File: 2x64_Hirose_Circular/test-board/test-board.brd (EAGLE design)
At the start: 152.4 x 165.1 mm, 55 parts

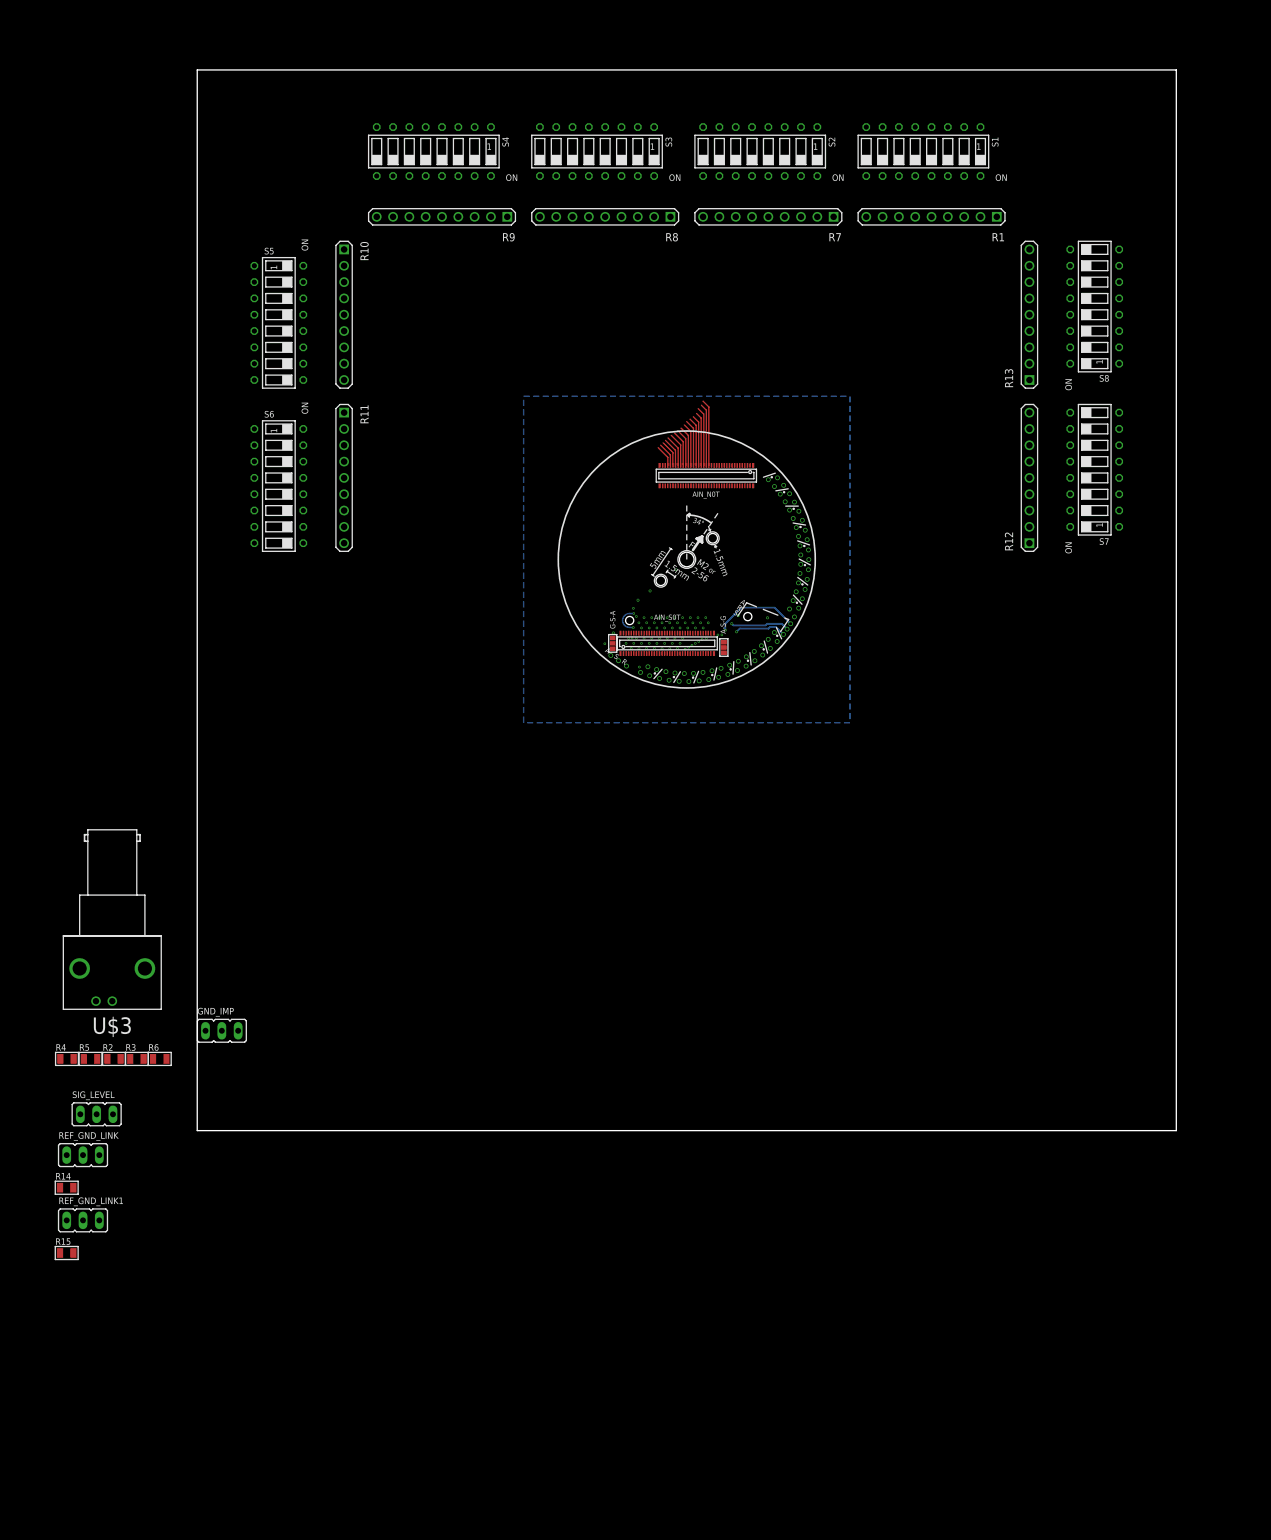
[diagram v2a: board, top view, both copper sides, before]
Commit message: Intial layout for 2x64 Hirose test board complete
- Silkscree needs work, especially for tetrode and channel labels, which
  will be very important
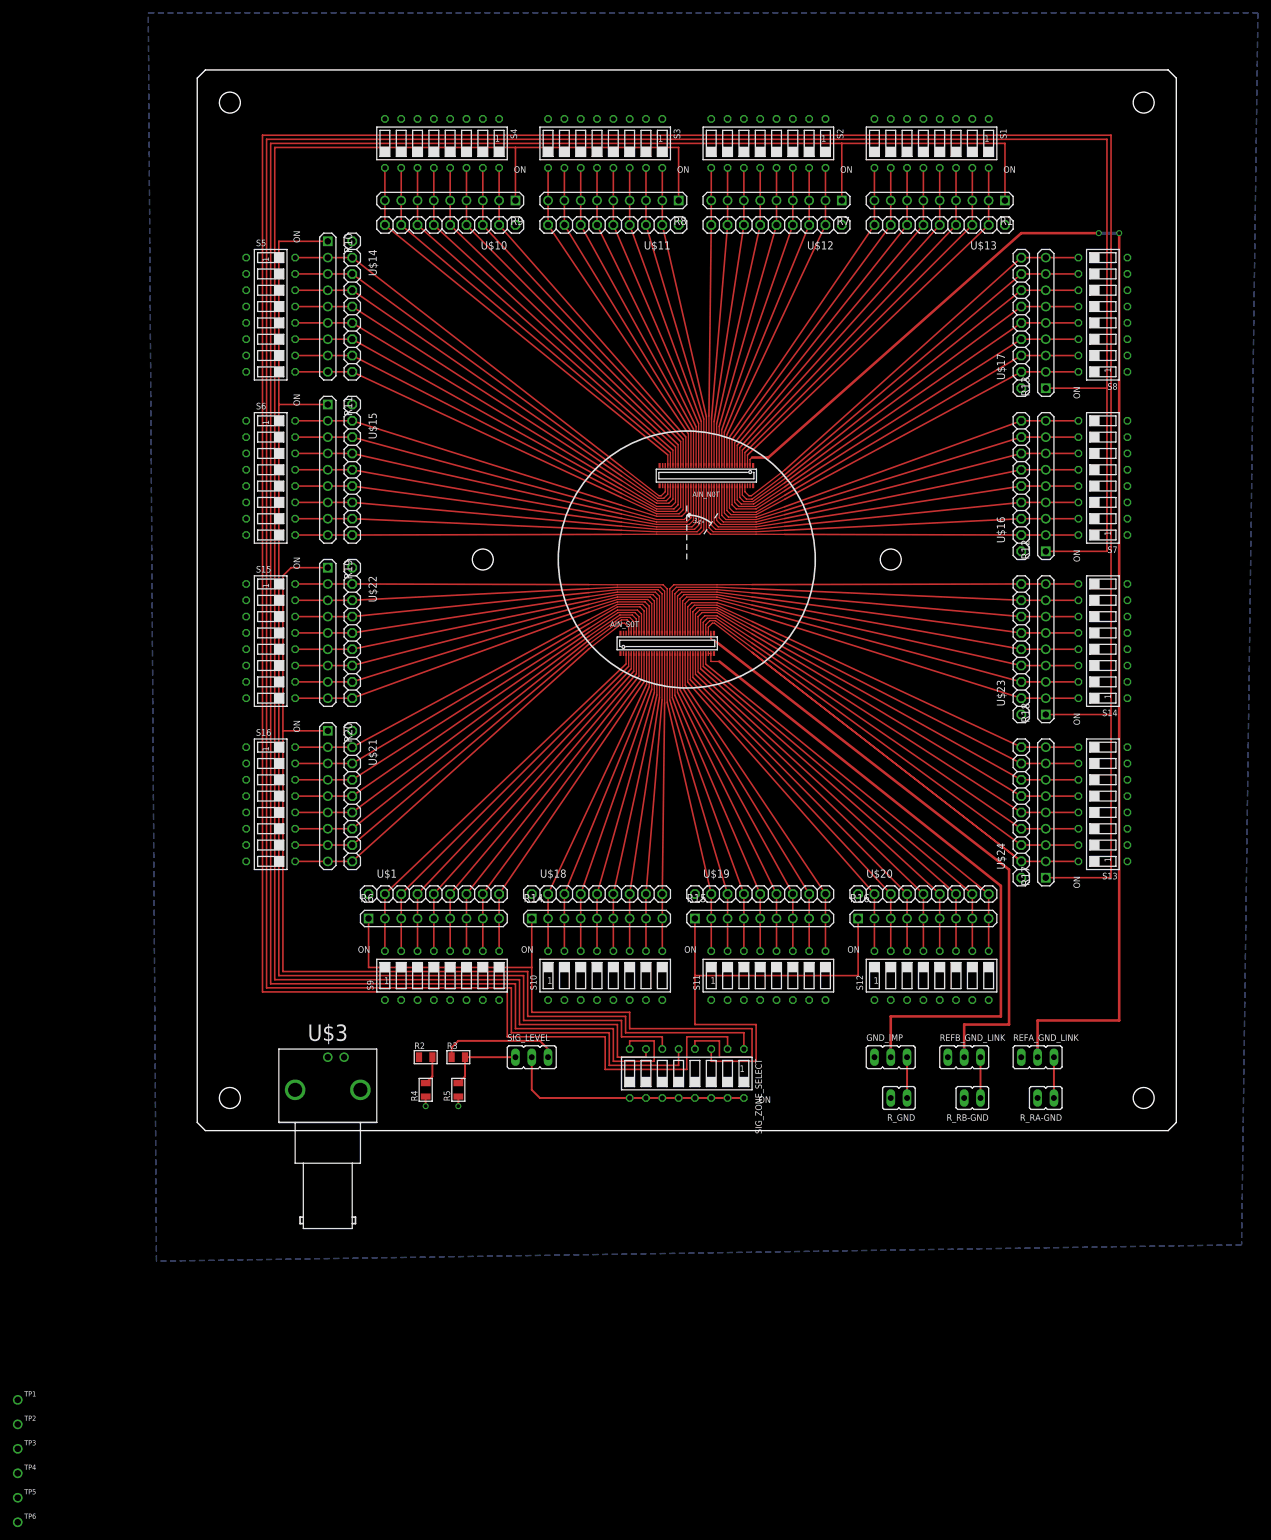
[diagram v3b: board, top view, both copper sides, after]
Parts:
- removed AGND_B0, AGND_B1, REF_B0, REF_B1, SHLD_B0, SHLD_B1: LRG_GP, jonnew:GOLDPIN_0.5ID_0.7OD
- removed REF_GND_LINK, REF_GND_LINK1: (no value), jonnew:JP3
- removed SJ_B0, SJ_B1: (no value), jonnew:SJ_2_0402
- removed TET16: 16, jonnew:TETRODE_128_0.5ID_0.7OD
- removed TET17: 17, jonnew:TETRODE_128_0.5ID_0.7OD
- removed TET18: 18, jonnew:TETRODE_128_0.5ID_0.7OD
- removed TET19: 19, jonnew:TETRODE_128_0.5ID_0.7OD
- removed TET20: 20, jonnew:TETRODE_128_0.5ID_0.7OD
- removed TET21: 21, jonnew:TETRODE_128_0.5ID_0.7OD
- removed TET22: 22, jonnew:TETRODE_128_0.5ID_0.7OD
- removed TET23: 23, jonnew:TETRODE_128_0.5ID_0.7OD
- removed TET24: 24, jonnew:TETRODE_128_0.5ID_0.7OD
- removed TET25: 25, jonnew:TETRODE_128_0.5ID_0.7OD
- removed TET26: 26, jonnew:TETRODE_128_0.5ID_0.7OD
- removed TET27: 27, jonnew:TETRODE_128_0.5ID_0.7OD
- removed TET28: 28, jonnew:TETRODE_128_0.5ID_0.7OD
- removed TET29: 29, jonnew:TETRODE_128_0.5ID_0.7OD
- removed TET30: 30, jonnew:TETRODE_128_0.5ID_0.7OD
- removed TET31: 31, jonnew:TETRODE_128_0.5ID_0.7OD
- added R16, R17, R18, R19, R20: 4609-220k, jonnew:RNX8-0.1
- added REFA_GND_LINK, REFB_GND_LINK: (no value), jonnew:JP3
- added R_GND, R_RA-GND, R_RB-GND: (no value), jonnew:JP2
- added S10, S11, S12, S13, S14, S15, S16, S9, SIG_ZONE_SELECT: (no value), jonnew:ADE008
- added TP1, TP2, TP3, TP4, TP5, TP6: (no value), jonnew:TESTPOINT
- added U$10, U$11, U$12, U$13, U$14, U$15, U$16, U$17, U$18, U$19, U$20, U$21, U$22, U$23, U$24: (no value), test-board:1X09
- AIN_S0T: device jonnew:DF40-70HEAD-EIB -> jonnew:DF40-70HEAD
- R14, R15, R6: value (none) -> 4609-220k; device jonnew:0805 -> jonnew:RNX8-0.1
- U$1: device jonnew:EIB_MOUNT_A -> test-board:1X09
- moved R15 110.8 mm to (1.27, -55.9)
- moved GND_IMP 104.2 mm to (29.2, -77.5)
- moved R14 83.6 mm to (-24.1, -55.9)
- moved U$1 70.1 mm to (-47.0, -52.1), turned to 0 degrees
- moved SIG_LEVEL 68.3 mm to (-26.7, -77.5)
- moved R5 57.5 mm to (-35.6, -82.5), turned to 90 degrees
- moved R4 56.0 mm to (-40.6, -82.5), turned to 90 degrees
- moved R3 50.0 mm to (-35.6, -77.5)
- moved R2 48.5 mm to (-40.6, -77.5)
- moved U$3 47.6 mm to (-50.8, -82.5), turned to 180 degrees
- moved R6 39.2 mm to (-49.5, -55.9)
- moved R1 2.84 mm to (49.5, 55.9)
- moved R10 2.84 mm to (-55.9, 49.5)
- moved R11 2.84 mm to (-55.9, 24.1)
- moved R12 2.84 mm to (55.9, 1.27)
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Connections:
- removed net AGND_B0: AGND_B0.P$1, AIN_S0T.69, AIN_S0T.70, SJ_B0.2
- removed net AGND_B1: AGND_B1.P$1, AIN_S0T.34, AIN_S0T.35, SJ_B1.2
- removed net N$1: R14.1, REF_GND_LINK.1
- removed net N$104: AIN_S0T.46, AIN_S0T.P46, TET26.2
- removed net N$105: AIN_S0T.47, AIN_S0T.P47, TET26.1
- removed net N$106: AIN_S0T.48, AIN_S0T.P48, TET26.0
- removed net N$107: AIN_S0T.49, AIN_S0T.P49, TET27.3
- removed net N$108: AIN_S0T.50, AIN_S0T.P50, TET27.2
- removed net N$109: AIN_S0T.51, AIN_S0T.P51, TET27.1
- removed net N$111: AIN_S0T.53, AIN_S0T.P53, TET28.3
- removed net N$112: AIN_S0T.54, AIN_S0T.P54, TET28.2
- removed net N$113: AIN_S0T.55, AIN_S0T.P55, TET28.1
- removed net N$114: AIN_S0T.56, AIN_S0T.P56, TET28.0
- removed net N$115: AIN_S0T.57, AIN_S0T.P57, TET29.3
- removed net N$116: AIN_S0T.58, AIN_S0T.P58, TET29.2
- removed net N$117: AIN_S0T.59, AIN_S0T.P59, TET29.1
- removed net N$118: AIN_S0T.60, AIN_S0T.P60, TET29.0
- removed net N$119: AIN_S0T.61, AIN_S0T.P61, TET30.3
- removed net N$120: AIN_S0T.62, AIN_S0T.P62, TET30.2
- removed net N$121: AIN_S0T.63, AIN_S0T.P63, TET30.1
- removed net N$122: AIN_S0T.64, AIN_S0T.P64, TET30.0
- removed net N$123: AIN_S0T.65, TET31.3
- removed net N$124: AIN_S0T.66, TET31.2
- removed net N$125: AIN_S0T.67, TET31.1
- removed net N$126: AIN_S0T.68, TET31.0
- removed net N$127: AIN_S0T.2, AIN_S0T.P2, TET16.3
- removed net N$128: AIN_S0T.37, AIN_S0T.P37, TET24.3
- removed net N$14: GND_IMP.1, R6.1
- removed net N$16: R4.1
- removed net N$17: R5.1
- removed net N$22: R15.1, REF_GND_LINK1.1
- removed net N$5: U$3.P$GND
- removed net N$96: AIN_S0T.38, AIN_S0T.P38, TET24.2
- removed net REF_B0: AIN_S0T.1, REF_B0.P$1
- removed net REF_B1: AIN_S0T.36, REF_B1.P$1
- new net N$130: AIN_S0T.62, R20.2, S16.15, U$21.2
- new net N$26: AIN_S0T.7, R6.6, S9.11, U$1.6
- new net N$32: AIN_S0T.9, R6.8, S9.9, U$1.8
- new net N$35: AIN_S0T.10, R14.1, S10.16, U$18.1
- new net N$41: AIN_S0T.11, R14.2, S10.15, U$18.2
- new net N$45: AIN_S0T.14, R14.5, S10.12, U$18.5
- new net N$46: AIN_S0T.15, R14.6, S10.11, U$18.6
- new net N$48: AIN_S0T.16, R14.7, S10.10, U$18.7
- new net N$49: AIN_S0T.19, R15.2, S11.15, U$19.2
- new net N$50: AIN_S0T.20, R15.3, S11.14, U$19.3
- new net N$51: AIN_S0T.21, R15.4, S11.13, U$19.4
- new net N$52: AIN_S0T.22, R15.5, S11.12, U$19.5
- new net N$53: AIN_S0T.23, R15.6, S11.11, U$19.6
- new net N$54: AIN_S0T.24, R15.7, S11.10, U$19.7
- new net N$55: AIN_S0T.25, R15.8, S11.9, U$19.8
- new net N$56: AIN_S0T.26, R16.1, S12.16, U$20.1
- new net N$58: AIN_S0T.27, R16.2, S12.15, U$20.2
- new net N$59: AIN_S0T.28, R16.3, S12.14, U$20.3
- new net N$60: AIN_S0T.29, R16.4, S12.13, U$20.4
- new net N$61: AIN_S0T.30, R16.5, S12.12, U$20.5
- new net N$62: AIN_S0T.31, R16.6, S12.11, U$20.6
- new net N$63: AIN_S0T.32, R16.7, S12.10, U$20.7
- new net N$64: AIN_S0T.33, R16.8, S12.9, U$20.8
- new net SIG_A_15-0: R12.C, R13.C, SIG_ZONE_SELECT.5
- new net SIG_A_31-16: R10.C, R11.C, SIG_ZONE_SELECT.6
- new net SIG_A_47-32: R8.C, R9.C, SIG_ZONE_SELECT.7
- new net SIG_A_63-48: R1.C, R7.C, SIG_ZONE_SELECT.8
- new net SIG_B_15-0: R19.C, R20.C, SIG_ZONE_SELECT.1
- new net SIG_B_31-16: R17.C, R18.C, SIG_ZONE_SELECT.2
- new net SIG_B_47-32: R15.C, R16.C, SIG_ZONE_SELECT.3
- new net SIG_B_63-48: R14.C, R6.C, SIG_ZONE_SELECT.4
- net GND: now also GND_IMP.1, R4.1, R5.1, REFA_GND_LINK.1, REFB_GND_LINK.1, R_GND.2, R_RA-GND.2, R_RB-GND.2, S10.1, S10.2, S10.3, S10.4, S10.5, S10.6, S10.7, S10.8, S11.1, S11.2, S11.3, S11.4, S11.5, S11.6, S11.7, S11.8, S12.1, S12.2, S12.3, S12.4, S12.5, S12.6, S12.7, S12.8, S13.1, S13.2, S13.3, S13.4, S13.5, S13.6, S13.7, S13.8, S14.1, S14.2, S14.3, S14.4, S14.5, S14.6, S14.7, S14.8, S15.1, S15.2, S15.3, S15.4, S15.5, S15.6, S15.7, S15.8, S16.1, S16.2, S16.3, S16.4, S16.5, S16.6, S16.7, S16.8, S9.1, S9.2, S9.3, S9.4, S9.5, S9.6, S9.7, S9.8, TP1.1, TP2.1, U$1.9, U$10.9, U$11.9, U$12.9, U$13.9, U$14.9, U$15.9, U$16.9, U$17.9, U$18.9, U$19.9, U$20.9, U$21.9, U$22.9, U$23.9, U$24.9, U$3.P$GND; no longer SJ_B0.1, SJ_B1.1
- net HS_GND: now also AIN_S0T.34, AIN_S0T.35; no longer AIN_N0T.34, AIN_N0T.35, AIN_N0T.69, AIN_N0T.70
- net N$10: now also U$13.2
- net N$100: now also AIN_S0T.54, R19.2, S15.15, U$22.2; no longer AIN_S0T.42, AIN_S0T.P42, TET25.2
- net N$101: now also AIN_S0T.56, R19.4, S15.13, U$22.4; no longer AIN_S0T.43, AIN_S0T.P43, TET25.1
- net N$102: now also AIN_S0T.58, R19.6, S15.11, U$22.6; no longer AIN_S0T.44, AIN_S0T.P44, TET25.0
- net N$103: now also AIN_S0T.59, R19.7, S15.10, U$22.7; no longer AIN_S0T.45, AIN_S0T.P45, TET26.3
- net N$11: now also U$12.3
- net N$110: now also AIN_S0T.13, R14.4, S10.13, U$18.4; no longer AIN_S0T.52, AIN_S0T.P52, TET27.0
- net N$12: now also U$13.3
- net N$13: now also U$12.1
- net N$15: now also REFA_GND_LINK.3, R_RA-GND.1; no longer GND_IMP.3, R6.2
- net N$18: now also U$13.6
- net N$19: now also U$13.7
- net N$2: now also GND_IMP.3, R_GND.1; no longer R14.2, REF_GND_LINK.3
- net N$20: now also U$13.5
- net N$206: now also U$10.1
- net N$207: now also U$11.8
- net N$21: now also U$13.1
- net N$210: now also U$11.5
- net N$212: now also U$11.3
- net N$214: now also U$11.1
- net N$216: now also U$12.7
- net N$219: now also U$12.4
- net N$221: now also U$12.2
- net N$23: now also U$10.2
- net N$230: now also U$13.4
- net N$231: now also U$14.2
- net N$233: now also U$14.4
- net N$235: now also U$14.6
- net N$237: now also U$14.8
- net N$238: now also U$15.1
- net N$239: now also U$15.2
- net N$24: now also U$10.4
- net N$241: now also U$15.4
- net N$242: now also U$15.5
- net N$243: now also U$15.6
- net N$245: now also U$15.7
- net N$247: now also U$16.2
- net N$248: now also U$16.3
- net N$249: now also U$16.4
- net N$25: now also U$14.7
- net N$250: now also U$16.5
- net N$251: now also U$16.6
- net N$252: now also U$16.7
- net N$253: now also U$16.8
- net N$254: now also U$17.1
- net N$255: now also U$17.2
- net N$256: now also U$17.3
- net N$257: now also U$17.4
- net N$258: now also U$17.5
- net N$259: now also U$17.6
- net N$260: now also U$17.7
- net N$261: now also U$17.8
- net N$27: now also U$10.7
- net N$28: now also REFB_GND_LINK.3, R_RB-GND.1; no longer R15.2, REF_GND_LINK1.3
- net N$29: now also U$10.5
- net N$3: now also AIN_S0T.3, R6.2, S9.15, U$1.2; no longer SHLD_B0.P$1, SJ_B0.COM
- net N$30: now also U$14.5
- net N$31: now also U$10.3
- net N$33: now also U$14.3
- net N$34: now also U$10.6
- net N$36: now also U$10.8
- net N$37: now also U$14.1
- net N$38: now also U$11.2
- net N$39: now also U$15.8
- net N$4: now also AIN_S0T.5, R6.4, S9.13, U$1.4; no longer SHLD_B1.P$1, SJ_B1.COM
- net N$40: now also U$11.4
- net N$42: now also U$11.6
- net N$43: now also U$11.7
- net N$47: now also U$15.3
- net N$57: now also U$16.1
- net N$6: now also U$12.8
- net N$65: now also AIN_S0T.8, R6.7, S9.10, U$1.7; no longer AIN_S0T.33, TET23.0
- net N$66: now also AIN_S0T.6, R6.5, S9.12, U$1.5; no longer AIN_S0T.32, TET23.1
- net N$67: now also AIN_S0T.4, R6.3, S9.14, U$1.3; no longer AIN_S0T.31, AIN_S0T.P31, TET23.2
- net N$68: now also AIN_S0T.2, R6.1, S9.16, U$1.1; no longer AIN_S0T.30, AIN_S0T.P30, TET23.3
- net N$69: now also AIN_S0T.17, R14.8, S10.9, U$18.8; no longer AIN_S0T.29, AIN_S0T.P29, TET22.0
- net N$7: now also U$13.8
- net N$70: now also AIN_S0T.12, R14.3, S10.14, U$18.3; no longer AIN_S0T.28, AIN_S0T.P28, TET22.1
- net N$71: now also AIN_S0T.18, R15.1, S11.16, U$19.1; no longer AIN_S0T.27, AIN_S0T.P27, TET22.2
- net N$72: now also AIN_S0T.61, R20.1, S16.16, U$21.1; no longer AIN_S0T.26, AIN_S0T.P26, TET22.3
- net N$73: now also AIN_S0T.60, R19.8, S15.9, U$22.8; no longer AIN_S0T.25, AIN_S0T.P25, TET21.0
- net N$74: now also AIN_S0T.57, R19.5, S15.12, U$22.5; no longer AIN_S0T.24, AIN_S0T.P24, TET21.1
- net N$75: now also AIN_S0T.55, R19.3, S15.14, U$22.3; no longer AIN_S0T.23, AIN_S0T.P23, TET21.2
- net N$76: now also AIN_S0T.53, R19.1, S15.16, U$22.1; no longer AIN_S0T.22, AIN_S0T.P22, TET21.3
- net N$77: now also AIN_S0T.51, R18.7, S14.10, U$23.7; no longer AIN_S0T.21, AIN_S0T.P21, TET20.0
- net N$78: now also AIN_S0T.48, R18.4, S14.13, U$23.4; no longer AIN_S0T.20, AIN_S0T.P20, TET20.1
- net N$79: now also AIN_S0T.46, R18.2, S14.15, U$23.2; no longer AIN_S0T.19, AIN_S0T.P19, TET20.2
- net N$8: now also U$12.6
- net N$80: now also AIN_S0T.40, R17.4, S13.13, U$24.4; no longer AIN_S0T.18, AIN_S0T.P18, TET20.3
- net N$81: now also AIN_S0T.52, R18.8, S14.9, U$23.8; no longer AIN_S0T.17, AIN_S0T.P17, TET19.0
- net N$82: now also AIN_S0T.50, R18.6, S14.11, U$23.6; no longer AIN_S0T.16, AIN_S0T.P16, TET19.1
- net N$83: now also AIN_S0T.49, R18.5, S14.12, U$23.5; no longer AIN_S0T.15, AIN_S0T.P15, TET19.2
- net N$84: now also AIN_S0T.47, R18.3, S14.14, U$23.3; no longer AIN_S0T.14, AIN_S0T.P14, TET19.3
- net N$85: now also AIN_S0T.45, R18.1, S14.16, U$23.1; no longer AIN_S0T.13, AIN_S0T.P13, TET18.0
- net N$86: now also AIN_S0T.67, R20.7, S16.10, U$21.7; no longer AIN_S0T.12, AIN_S0T.P12, TET18.1
- net N$87: now also AIN_S0T.65, R20.5, S16.12, U$21.5; no longer AIN_S0T.11, AIN_S0T.P11, TET18.2
- net N$88: now also AIN_S0T.63, R20.3, S16.14, U$21.3; no longer AIN_S0T.10, AIN_S0T.P10, TET18.3
- net N$89: now also AIN_S0T.44, R17.8, S13.9, U$24.8; no longer AIN_S0T.9, AIN_S0T.P9, TET17.0
- net N$9: now also U$12.5
- net N$90: now also AIN_S0T.38, R17.2, S13.15, U$24.2; no longer AIN_S0T.8, AIN_S0T.P8, TET17.1
- net N$91: now also AIN_S0T.39, R17.3, S13.14, U$24.3; no longer AIN_S0T.7, AIN_S0T.P7, TET17.2
- net N$92: now also AIN_S0T.42, R17.6, S13.11, U$24.6; no longer AIN_S0T.6, AIN_S0T.P6, TET17.3
- net N$93: now also AIN_S0T.43, R17.7, S13.10, U$24.7; no longer AIN_S0T.5, AIN_S0T.P5, TET16.0
- net N$94: now also AIN_S0T.41, R17.5, S13.12, U$24.5; no longer AIN_S0T.4, AIN_S0T.P4, TET16.1
- net N$95: now also AIN_S0T.37, R17.1, S13.16, U$24.1; no longer AIN_S0T.3, AIN_S0T.P3, TET16.2
- net N$97: now also AIN_S0T.64, R20.4, S16.13, U$21.4; no longer AIN_S0T.39, AIN_S0T.P39, TET24.1
- net N$98: now also AIN_S0T.66, R20.6, S16.11, U$21.6; no longer AIN_S0T.40, AIN_S0T.P40, TET24.0
- net N$99: now also AIN_S0T.68, R20.8, S16.9, U$21.8; no longer AIN_S0T.41, AIN_S0T.P41, TET25.3
- net REF_A: now also REFA_GND_LINK.2; no longer AIN_N0T.36, REF_GND_LINK.2
- net REF_B: now also AIN_S0T.36, REFB_GND_LINK.2; no longer REF_GND_LINK1.2
- net SIG: now also SIG_ZONE_SELECT.10, SIG_ZONE_SELECT.11, SIG_ZONE_SELECT.12, SIG_ZONE_SELECT.13, SIG_ZONE_SELECT.14, SIG_ZONE_SELECT.15, SIG_ZONE_SELECT.16, SIG_ZONE_SELECT.9; no longer R1.C, R10.C, R11.C, R12.C, R13.C, R7.C, R8.C, R9.C
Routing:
- net SIG_B_31-16: track 0.00 -> 492.8 mm
- net SIG_A_15-0: track 0.00 -> 424.8 mm
- net SIG_A_63-48: track 0.00 -> 342.9 mm
- net SIG_A_47-32: track 0.00 -> 280.0 mm
- net REF_A: track 0.00 -> 212.7 mm, vias 0 -> 2
- net SIG_A_31-16: track 0.00 -> 200.7 mm
- net SIG_B_15-0: track 0.00 -> 159.9 mm
- net N$95: track 6.41 -> 124.6 mm
- net HS_GND: track 0.00 -> 102.8 mm
- net SIG_B_63-48: track 0.00 -> 101.6 mm
- net REF_B: track 0.00 -> 95.7 mm
- net SIG_B_47-32: track 0.00 -> 75.6 mm
- net N$37: track 0.00 -> 71.5 mm
- net N$231: track 0.00 -> 71.0 mm
- net N$39: track 0.00 -> 70.8 mm
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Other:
- outline, holes or cut-outs redrawn
- board text removed: "A"
- board text removed: "A-S-G"
- board text removed: "G-S-A"
- board text removed: "R"
- board text removed: "S"

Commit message: Pretty much done with layout. Do ERC and gerber verification.
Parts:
- removed REFA_GND_LINK, REFB_GND_LINK, SIG_LEVEL: (no value), jonnew:JP3
- removed SIG_ZONE_SELECT: (no value), jonnew:ADE008
- removed U$18, U$19, U$20, U$22, U$23, U$24: (no value), test-board:1X09
- added BANK_SELECT: KAT1108E, jonnew:206-124_DIP8-SPDT
- added REFA_TO_GND, REFB_TO_GND, SIG_GAIN: (no value), jonnew:JP3
- added SIG_IN: 1-1634622-0, josh:BNC_RIGHT_ANGLE
- added TP10, TP11, TP12, TP13: TP_4-40, jonnew:4-40_PLATED
- added TP7: SIG_IN, jonnew:P1-20
- added TP8: -40dB, jonnew:P1-20
- added TP9: -80dB, jonnew:P1-20
- added U$2, U$4, U$5, U$6, U$7: (no value), test-board:1X09
- R1, R10, R11, R12, R13, R14, R15, R16, R6, R7, R8, R9: value 4609-220k -> 4609
- R17, R18: value 4609-220k -> 10k; device jonnew:RNX8-0.1 -> jonnew:0805
- R19, R20: value 4609-220k -> 100; device jonnew:RNX8-0.1 -> jonnew:0805
- R2, R3: value 10k -> 4609; device jonnew:0805 -> jonnew:RNX8-0.1
- R4, R5: value 100 -> 4609; device jonnew:0805 -> jonnew:RNX8-0.1
- S1, S10, S11, S12, S13, S14, S15, S16, S2, S3, S4, S5, S6, S7, S8, S9: device jonnew:ADE008 -> jonnew:ADE_DIP8-SPST
- TP1, TP2, TP3, TP4, TP5, TP6: value (none) -> GND; device jonnew:TESTPOINT -> jonnew:P1-20
- U$3: value BNC_RIGHT_ANGLE -> (none); device josh:BNC_RIGHT_ANGLE -> test-board:1X09
- moved TP4 261.4 mm to (60.3, 61.0)
- moved TP6 209.3 mm to (41.9, 0.00)
- moved TP3 201.1 mm to (-57.1, 57.1)
- moved TP2 179.6 mm to (67.3, -81.3)
- moved R4 165.2 mm to (49.5, 55.9), turned to 180 degrees
- moved TP5 158.8 mm to (-41.9, 0.00)
- moved U$3 152.8 mm to (21.6, 52.1)
- moved R3 146.1 mm to (24.1, 55.9), turned to 180 degrees
- moved U$13 140.3 mm to (-47.0, -52.1), turned to 0 degrees
- moved R2 139.0 mm to (-1.27, 55.9), turned to 180 degrees
- moved R13 133.9 mm to (-49.5, -55.9), turned to 0 degrees
- moved R5 133.6 mm to (-55.9, 49.5), turned to 270 degrees
- moved R11 121.7 mm to (55.9, -24.1), turned to 90 degrees
- moved S13 106.3 mm to (-38.1, -64.8), turned to 0 degrees
- moved S16 106.3 mm to (38.1, -64.8), turned to 0 degrees
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- renumbered U$17 to U$8, U$21 to U$9
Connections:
- removed net SIG_A_15-0: R12.C, R13.C, SIG_ZONE_SELECT.5
- removed net SIG_A_31-16: R10.C, R11.C, SIG_ZONE_SELECT.6
- removed net SIG_A_47-32: R8.C, R9.C, SIG_ZONE_SELECT.7
- removed net SIG_A_63-48: R1.C, R7.C, SIG_ZONE_SELECT.8
- removed net SIG_B_15-0: R19.C, R20.C, SIG_ZONE_SELECT.1
- removed net SIG_B_31-16: R17.C, R18.C, SIG_ZONE_SELECT.2
- removed net SIG_B_47-32: R15.C, R16.C, SIG_ZONE_SELECT.3
- removed net SIG_B_63-48: R14.C, R6.C, SIG_ZONE_SELECT.4
- new net SIG_N_15-0: BANK_SELECT.4, R7.C, R8.C
- new net SIG_N_31-16: BANK_SELECT.3, R5.C, R6.C
- new net SIG_N_47-32: BANK_SELECT.2, R1.C, R2.C
- new net SIG_N_63-48: BANK_SELECT.1, R3.C, R4.C
- new net SIG_S_15-0: BANK_SELECT.8, R10.C, R9.C
- new net SIG_S_31-16: BANK_SELECT.7, R11.C, R12.C
- new net SIG_S_47-32: BANK_SELECT.6, R15.C, R16.C
- new net SIG_S_63-48: BANK_SELECT.5, R13.C, R14.C
- net -40DB: now also R17.2, R18.1, R19.2, SIG_GAIN.3, TP8.TP; no longer R2.2, R3.1, R4.2, SIG_LEVEL.3
- net -80DB: now also R18.2, R20.2, SIG_GAIN.1, TP9.TP; no longer R3.2, R5.2, SIG_LEVEL.1
- net GND: now also BANK_SELECT.-, R19.1, R20.1, REFA_TO_GND.1, REFB_TO_GND.1, SIG_IN.P$GND, TP1.TP, TP10.P$1, TP11.P$1, TP12.P$1, TP13.P$1, TP2.TP, TP3.TP, TP4.TP, TP5.TP, TP6.TP, U$2.9, U$3.9, U$4.9, U$5.9, U$6.9, U$7.9; no longer R4.1, R5.1, REFA_GND_LINK.1, REFB_GND_LINK.1, TP1.1, TP2.1, U$18.9, U$19.9, U$20.9, U$22.9, U$23.9, U$24.9, U$3.P$GND
- net N$10: now also R4.2, S4.15, U$4.2; no longer R1.2, S1.15, U$13.2
- net N$100: now also R10.2, S10.15, U$10.2; no longer R19.2, S15.15, U$22.2
- net N$101: now also R10.4, S10.13, U$10.4; no longer R19.4, S15.13, U$22.4
- net N$102: now also R10.6, S10.11, U$10.6; no longer R19.6, S15.11, U$22.6
- net N$103: now also R10.7, S10.10, U$10.7; no longer R19.7, S15.10, U$22.7
- net N$11: now also R3.3, S3.14, U$3.3; no longer R7.3, S2.14, U$12.3
- net N$110: now also S14.13, U$14.4; no longer S10.13, U$18.4
- net N$12: now also R4.3, S4.14, U$4.3; no longer R1.3, S1.14, U$13.3
- net N$13: now also R3.1, S3.16, U$3.1; no longer R7.1, S2.16, U$12.1
- net N$130: now also R9.2, S9.15; no longer R20.2, S16.15
- net N$15: now also REFA_TO_GND.3; no longer REFA_GND_LINK.3
- net N$18: now also R4.6, S4.11, U$4.6; no longer R1.6, S1.11, U$13.6
- net N$19: now also R4.7, S4.10, U$4.7; no longer R1.7, S1.10, U$13.7
- net N$20: now also R4.5, S4.12, U$4.5; no longer R1.5, S1.12, U$13.5
- net N$206: now also R1.1, S1.16, U$1.1; no longer R9.1, S4.16, U$10.1
- net N$207: now also R2.8, S2.9, U$2.8; no longer R8.8, S3.9, U$11.8
- net N$21: now also R4.1, S4.16, U$4.1; no longer R1.1, S1.16, U$13.1
- net N$210: now also R2.5, S2.12, U$2.5; no longer R8.5, S3.12, U$11.5
- net N$212: now also R2.3, S2.14, U$2.3; no longer R8.3, S3.14, U$11.3
- net N$214: now also R2.1, S2.16, U$2.1; no longer R8.1, S3.16, U$11.1
- net N$216: now also R3.7, S3.10, U$3.7; no longer R7.7, S2.10, U$12.7
- net N$219: now also R3.4, S3.13, U$3.4; no longer R7.4, S2.13, U$12.4
- net N$221: now also R3.2, S3.15, U$3.2; no longer R7.2, S2.15, U$12.2
- net N$23: now also R1.2, S1.15, U$1.2; no longer R9.2, S4.15, U$10.2
- net N$230: now also R4.4, S4.13, U$4.4; no longer R1.4, S1.13, U$13.4
- net N$231: now also R5.2, U$5.2; no longer R10.2, U$14.2
- net N$233: now also R5.4, U$5.4; no longer R10.4, U$14.4
- net N$235: now also R5.6, U$5.6; no longer R10.6, U$14.6
- net N$237: now also R5.8, U$5.8; no longer R10.8, U$14.8
- net N$238: now also R6.1, U$6.1; no longer R11.1, U$15.1
- net N$239: now also R6.2, U$6.2; no longer R11.2, U$15.2
- net N$24: now also R1.4, S1.13, U$1.4; no longer R9.4, S4.13, U$10.4
- net N$241: now also R6.4, U$6.4; no longer R11.4, U$15.4
- net N$242: now also R6.5, U$6.5; no longer R11.5, U$15.5
- net N$243: now also R6.6, U$6.6; no longer R11.6, U$15.6
- net N$245: now also R6.7, U$6.7; no longer R11.7, U$15.7
- net N$247: now also R7.2, U$7.2; no longer R12.2, U$16.2
- net N$248: now also R7.3, U$7.3; no longer R12.3, U$16.3
- net N$249: now also R7.4, U$7.4; no longer R12.4, U$16.4
- net N$25: now also R5.7, U$5.7; no longer R10.7, U$14.7
- net N$250: now also R7.5, U$7.5; no longer R12.5, U$16.5
- net N$251: now also R7.6, U$7.6; no longer R12.6, U$16.6
- net N$252: now also R7.7, U$7.7; no longer R12.7, U$16.7
- net N$253: now also R7.8, U$7.8; no longer R12.8, U$16.8
- net N$254: now also R8.1; no longer R13.1
- net N$255: now also R8.2; no longer R13.2
- net N$256: now also R8.3; no longer R13.3
- net N$257: now also R8.4; no longer R13.4
- net N$258: now also R8.5; no longer R13.5
- net N$259: now also R8.6; no longer R13.6
- net N$26: now also R13.6, S13.11, U$13.6; no longer R6.6, S9.11, U$1.6
- net N$260: now also R8.7; no longer R13.7
- net N$261: now also R8.8; no longer R13.8
- net N$27: now also R1.7, S1.10, U$1.7; no longer R9.7, S4.10, U$10.7
- net N$28: now also REFB_TO_GND.3; no longer REFB_GND_LINK.3
- net N$29: now also R1.5, S1.12, U$1.5; no longer R9.5, S4.12, U$10.5
- net N$3: now also R13.2, S13.15, U$13.2; no longer R6.2, S9.15, U$1.2
- net N$30: now also R5.5, U$5.5; no longer R10.5, U$14.5
- net N$31: now also R1.3, S1.14, U$1.3; no longer R9.3, S4.14, U$10.3
- net N$32: now also R13.8, S13.9, U$13.8; no longer R6.8, S9.9, U$1.8
- net N$33: now also R5.3, U$5.3; no longer R10.3, U$14.3
- net N$34: now also R1.6, S1.11, U$1.6; no longer R9.6, S4.11, U$10.6
- net N$35: now also S14.16, U$14.1; no longer S10.16, U$18.1
- net N$36: now also R1.8, S1.9, U$1.8; no longer R9.8, S4.9, U$10.8
- net N$37: now also R5.1, U$5.1; no longer R10.1, U$14.1
- net N$38: now also R2.2, S2.15, U$2.2; no longer R8.2, S3.15, U$11.2
- net N$39: now also R6.8, U$6.8; no longer R11.8, U$15.8
- net N$4: now also R13.4, S13.13, U$13.4; no longer R6.4, S9.13, U$1.4
- net N$40: now also R2.4, S2.13, U$2.4; no longer R8.4, S3.13, U$11.4
- net N$41: now also S14.15, U$14.2; no longer S10.15, U$18.2
- net N$42: now also R2.6, S2.11, U$2.6; no longer R8.6, S3.11, U$11.6
- net N$43: now also R2.7, S2.10, U$2.7; no longer R8.7, S3.10, U$11.7
- net N$45: now also S14.12, U$14.5; no longer S10.12, U$18.5
- net N$46: now also S14.11, U$14.6; no longer S10.11, U$18.6
- net N$47: now also R6.3, U$6.3; no longer R11.3, U$15.3
- net N$48: now also S14.10, U$14.7; no longer S10.10, U$18.7
- net N$49: now also S15.15, U$15.2; no longer S11.15, U$19.2
- net N$50: now also S15.14, U$15.3; no longer S11.14, U$19.3
- net N$51: now also S15.13, U$15.4; no longer S11.13, U$19.4
- net N$52: now also S15.12, U$15.5; no longer S11.12, U$19.5
- net N$53: now also S15.11, U$15.6; no longer S11.11, U$19.6
- net N$54: now also S15.10, U$15.7; no longer S11.10, U$19.7
- net N$55: now also S15.9, U$15.8; no longer S11.9, U$19.8
- net N$56: now also S16.16, U$16.1; no longer S12.16, U$20.1
- net N$57: now also R7.1, U$7.1; no longer R12.1, U$16.1
- net N$58: now also S16.15, U$16.2; no longer S12.15, U$20.2
- net N$59: now also S16.14, U$16.3; no longer S12.14, U$20.3
- net N$6: now also R3.8, S3.9, U$3.8; no longer R7.8, S2.9, U$12.8
- net N$60: now also S16.13, U$16.4; no longer S12.13, U$20.4
- net N$61: now also S16.12, U$16.5; no longer S12.12, U$20.5
- net N$62: now also S16.11, U$16.6; no longer S12.11, U$20.6
- net N$63: now also S16.10, U$16.7; no longer S12.10, U$20.7
- net N$64: now also S16.9, U$16.8; no longer S12.9, U$20.8
- net N$65: now also R13.7, S13.10, U$13.7; no longer R6.7, S9.10, U$1.7
- net N$66: now also R13.5, S13.12, U$13.5; no longer R6.5, S9.12, U$1.5
- net N$67: now also R13.3, S13.14, U$13.3; no longer R6.3, S9.14, U$1.3
- net N$68: now also R13.1, S13.16, U$13.1; no longer R6.1, S9.16, U$1.1
- net N$69: now also S14.9, U$14.8; no longer S10.9, U$18.8
- net N$7: now also R4.8, S4.9, U$4.8; no longer R1.8, S1.9, U$13.8
- net N$70: now also S14.14, U$14.3; no longer S10.14, U$18.3
- net N$71: now also S15.16, U$15.1; no longer S11.16, U$19.1
- net N$72: now also R9.1, S9.16; no longer R20.1, S16.16
- net N$73: now also R10.8, S10.9, U$10.8; no longer R19.8, S15.9, U$22.8
- net N$74: now also R10.5, S10.12, U$10.5; no longer R19.5, S15.12, U$22.5
- net N$75: now also R10.3, S10.14, U$10.3; no longer R19.3, S15.14, U$22.3
- net N$76: now also R10.1, S10.16, U$10.1; no longer R19.1, S15.16, U$22.1
- net N$77: now also R11.7, S11.10, U$11.7; no longer R18.7, S14.10, U$23.7
- net N$78: now also R11.4, S11.13, U$11.4; no longer R18.4, S14.13, U$23.4
- net N$79: now also R11.2, S11.15, U$11.2; no longer R18.2, S14.15, U$23.2
- net N$8: now also R3.6, S3.11, U$3.6; no longer R7.6, S2.11, U$12.6
- net N$80: now also R12.4, S12.13, U$12.4; no longer R17.4, S13.13, U$24.4
- net N$81: now also R11.8, S11.9, U$11.8; no longer R18.8, S14.9, U$23.8
- net N$82: now also R11.6, S11.11, U$11.6; no longer R18.6, S14.11, U$23.6
- net N$83: now also R11.5, S11.12, U$11.5; no longer R18.5, S14.12, U$23.5
- net N$84: now also R11.3, S11.14, U$11.3; no longer R18.3, S14.14, U$23.3
- net N$85: now also R11.1, S11.16, U$11.1; no longer R18.1, S14.16, U$23.1
- net N$86: now also R9.7, S9.10; no longer R20.7, S16.10
- net N$87: now also R9.5, S9.12; no longer R20.5, S16.12
- net N$88: now also R9.3, S9.14; no longer R20.3, S16.14
- net N$89: now also R12.8, S12.9, U$12.8; no longer R17.8, S13.9, U$24.8
- net N$9: now also R3.5, S3.12, U$3.5; no longer R7.5, S2.12, U$12.5
- net N$90: now also R12.2, S12.15, U$12.2; no longer R17.2, S13.15, U$24.2
- net N$91: now also R12.3, S12.14, U$12.3; no longer R17.3, S13.14, U$24.3
- net N$92: now also R12.6, S12.11, U$12.6; no longer R17.6, S13.11, U$24.6
- net N$93: now also R12.7, S12.10, U$12.7; no longer R17.7, S13.10, U$24.7
- net N$94: now also R12.5, S12.12, U$12.5; no longer R17.5, S13.12, U$24.5
- net N$95: now also R12.1, S12.16, U$12.1; no longer R17.1, S13.16, U$24.1
- net N$97: now also R9.4, S9.13; no longer R20.4, S16.13
- net N$98: now also R9.6, S9.11; no longer R20.6, S16.11
- net N$99: now also R9.8, S9.9; no longer R20.8, S16.9
- net REF_A: now also REFA_TO_GND.2; no longer REFA_GND_LINK.2
- net REF_B: now also REFB_TO_GND.2; no longer REFB_GND_LINK.2
- net SIG: now also BANK_SELECT.+, SIG_GAIN.2; no longer SIG_LEVEL.2, SIG_ZONE_SELECT.10, SIG_ZONE_SELECT.11, SIG_ZONE_SELECT.12, SIG_ZONE_SELECT.13, SIG_ZONE_SELECT.14, SIG_ZONE_SELECT.15, SIG_ZONE_SELECT.16, SIG_ZONE_SELECT.9
- net SIG_IN: now also R17.1, SIG_IN.P$SIG, TP7.TP; no longer R2.1, U$3.P$SIG
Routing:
- net SIG_B_31-16: track 492.8 -> 0.00 mm
- net SIG_S_31-16: track 0.00 -> 492.6 mm
- net SIG_N_15-0: track 0.00 -> 425.7 mm
- net SIG_A_15-0: track 424.8 -> 0.00 mm
- net SIG_N_63-48: track 0.00 -> 344.6 mm
- net SIG_A_63-48: track 342.9 -> 0.00 mm
- net SIG_N_47-32: track 0.00 -> 282.4 mm
- net SIG_A_47-32: track 280.0 -> 0.00 mm
- net SIG_N_31-16: track 0.00 -> 203.1 mm
- net SIG_A_31-16: track 200.7 -> 0.00 mm
- net SIG_S_15-0: track 0.00 -> 163.1 mm
- net SIG_B_15-0: track 159.9 -> 0.00 mm
- net SIG_S_63-48: track 0.00 -> 104.8 mm
- net SIG_B_63-48: track 101.6 -> 0.00 mm
- net SIG_S_47-32: track 0.00 -> 79.9 mm
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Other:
- board size 152.4 x 165.1 mm -> 152.4 x 168.9 mm
- board text added: "-40dB"
- board text added: "-80dB"
- board text added: "128 Channel Headstage Module Test Board"
- board text added: "GND"
- board text added: "N00"
- board text added: "N07"
- board text added: "N08"
- board text added: "N15"
- board text added: "N16"
- board text added: "N23"
- board text added: "N24"
- board text added: "N31"
- board text added: "N32"
- board text added: "N39"
- board text added: "N40"
- board text added: "N47"
- board text added: "N48"
- board text added: "N55"
- board text added: "N56"
- board text added: "N63"
- board text added: "NC"
- board text added: "NORTH"
- board text added: "N_00-15"
- board text added: "N_31-16"
- board text added: "N_47-32"
- board text added: "N_63-48"
- board text added: "Rev. 1.0 CC BY-SA-NC-4.0 JPN, MWL@MIT 2016-03"
- board text added: "S00"
- board text added: "S07"
- board text added: "S08"
- board text added: "S15"
- board text added: "S16"
- board text added: "S23"
- board text added: "S24"
- board text added: "S31"
- board text added: "S32"
- board text added: "S39"
- board text added: "S40"
- board text added: "S47"
- board text added: "S48"
- board text added: "S55"
- board text added: "S56"
- board text added: "S63"
- board text added: "SOUTH"
- board text added: "S_00-15"
- board text added: "S_31-16"
- board text added: "S_47-32"
- board text added: "S_63-48"
- board text added: "TT00"
- board text added: "TT01"
- board text added: "TT02"
- board text added: "TT03"
- board text added: "TT04"
- board text added: "TT05"
- board text added: "TT06"
- board text added: "TT07"
- board text added: "TT08"
- board text added: "TT09"
- board text added: "TT10"
- board text added: "TT11"
- board text added: "TT12"
- board text added: "TT13"
- board text added: "TT14"
- board text added: "TT15"
- board text added: "TT16"
- board text added: "TT17"
- board text added: "TT18"
- board text added: "TT19"
- board text added: "TT20"
- board text added: "TT21"
- board text added: "TT22"
- board text added: "TT23"
- board text added: "TT24"
- board text added: "TT25"
- board text added: "TT26"
- board text added: "TT27"
- board text added: "TT28"
- board text added: "TT29"
- board text added: "TT30"
- board text added: "TT31"
- board text removed: "128 Channel EIB"
- board text removed: "34°"
- board text removed: "Rev. 1.0 CC BY-SA-NC-4.0 JPN, MWL@MIT 2015-02"
